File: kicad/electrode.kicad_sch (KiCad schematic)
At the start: 0 parts

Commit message: mcu changed cuz of clock requierements
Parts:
- added C1: 0.1u, symbol Device:C
- added C2: 4.7u, symbol Device:C
- added U1: CH32L103K8U6, easyeda2kicad:QFN-32_L4.0-W4.0-P0.40-BL-EP2.7-A, symbol LIB:CH32L103K8U6
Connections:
- new net 3v3: C1.1, C2.1, U1.1 (VDD)
- new net GND: C1.2, C2.2, U1.33 (EP)

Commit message: new mcu with clk_out and layout draft
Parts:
- C1: footprint (none) -> Capacitor_SMD:C_0402_1005Metric
- C2: footprint (none) -> Capacitor_SMD:C_0603_1608Metric
- U1: footprint easyeda2kicad:QFN-32_L4.0-W4.0-P0.40-BL-EP2.7-A -> LIB:QFN-32_L4.0-W4.0-P0.40-BL-EP2.7-A
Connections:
- net CLK_OUT: now reaches U1.18 (PA8)
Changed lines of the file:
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@@
+	(wire
+		(pts
+			(xy 186.69 110.49) (xy 168.91 110.49)
+		)
+		(stroke
+			(width 0)
+			(type default)
+		)
+	)
 	(wire
 		(pts
@@
 			)
 			(justify right)
+		)
+	)
+	(hierarchical_label "CLK_OUT"
+		(shape input)
+		(at 186.69 110.49 0)
+		(effects
+			(font
+				(size 1.27 1.27)
+			)
+			(justify left)
 		)
 	)
@@
 			)
 		)
-		(property "Footprint" "easyeda2kicad:QFN-32_L4.0-W4.0-P0.40-BL-EP2.7-A"
+		(property "Footprint" "LIB:QFN-32_L4.0-W4.0-P0.40-BL-EP2.7-A"
 			(at 142.24 138.43 0)
 			(hide yes)
@@
 			)
 		)
-		(property "Footprint" ""
+		(property "Footprint" "Capacitor_SMD:C_0402_1005Metric"
 			(at 134.3152 44.45 0)
 			(hide yes)
@@
 			)
 		)
-		(property "Footprint" ""
+		(property "Footprint" "Capacitor_SMD:C_0603_1608Metric"
 			(at 149.5552 44.45 0)
 			(hide yes)

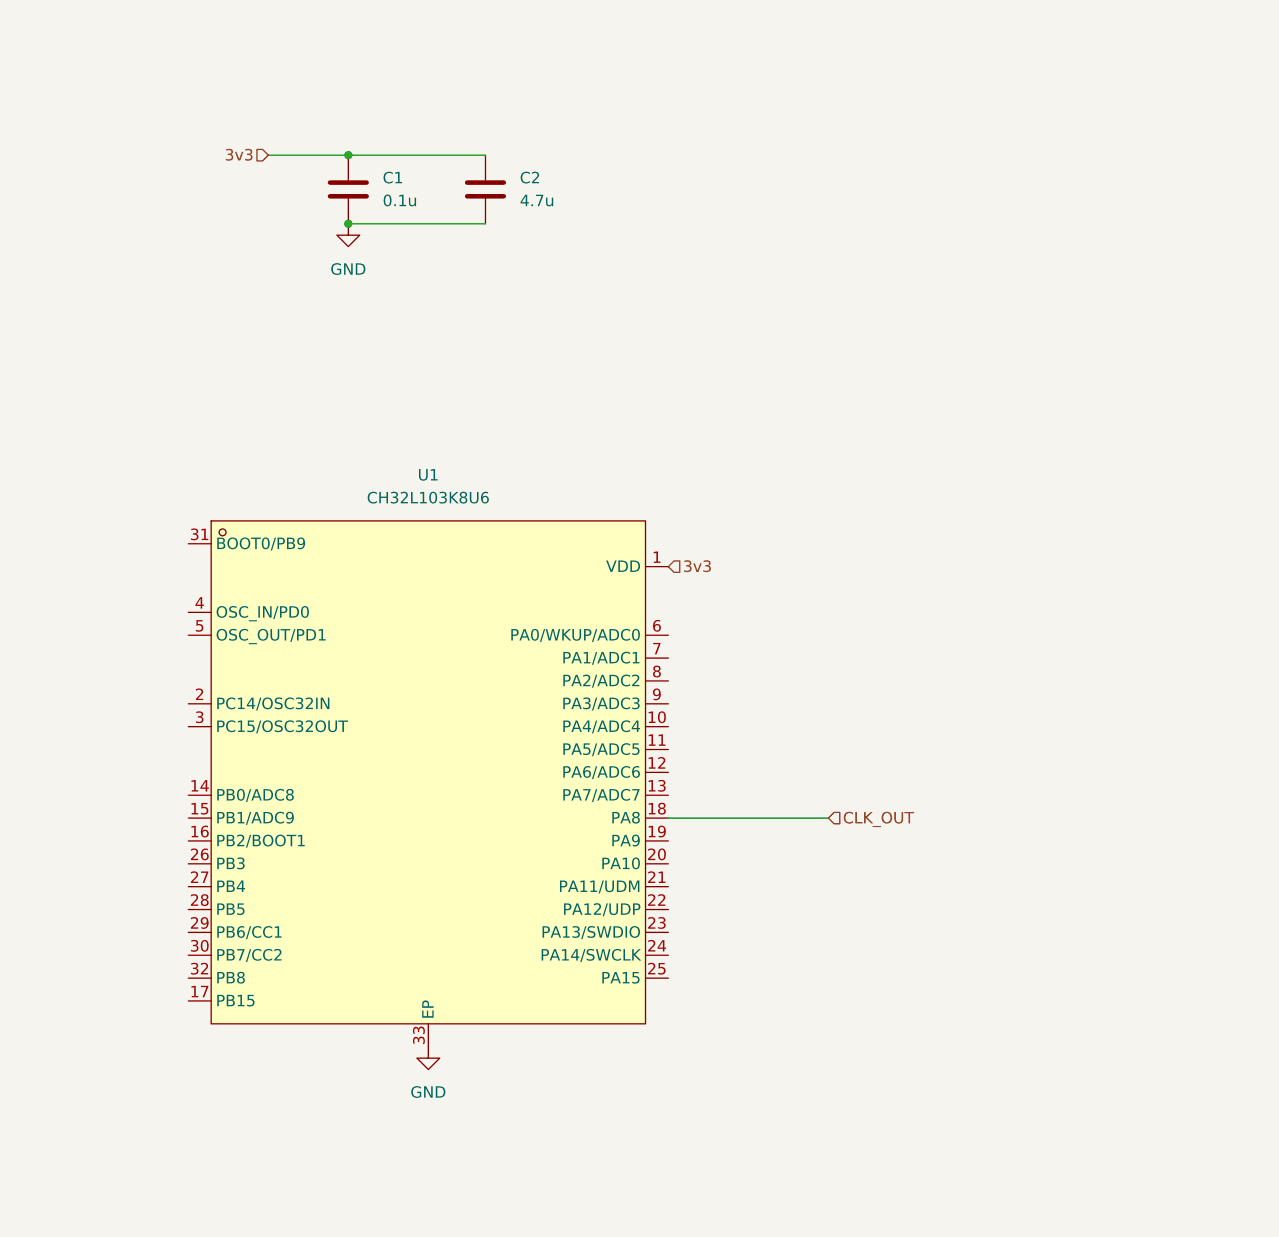
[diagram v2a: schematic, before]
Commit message: mcu chain test board with mcu side only for now
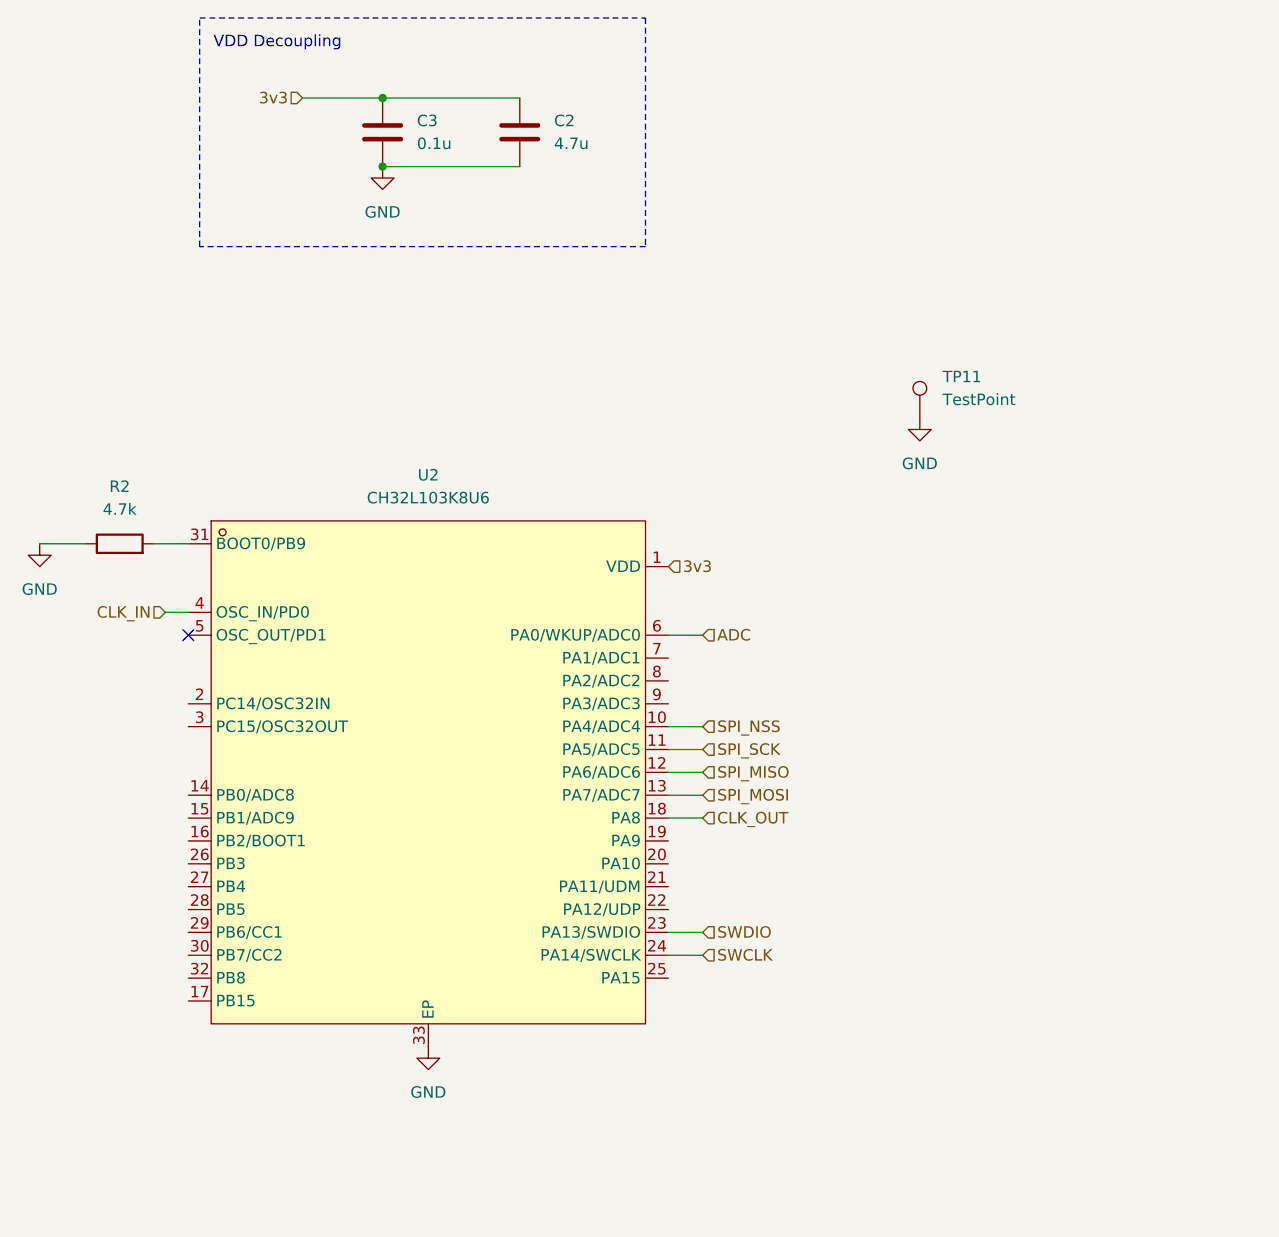
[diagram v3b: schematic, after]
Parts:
- added R2: 4.7k, symbol Device:R
- added TP11: TestPoint, symbol Connector:TestPoint
- renumbered C1 to C3, U1 to U2
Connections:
- net GND: now also R2.1, TP11.1
- net SPI_NSS: now reaches U2.10 (PA4/ADC4)
- net SPI_SCK: now reaches U2.11 (PA5/ADC5)
- net SPI_MISO: now reaches U2.12 (PA6/ADC6)
- net SPI_MOSI: now reaches U2.13 (PA7/ADC7)
- net SWDIO: now reaches U2.23 (PA13/SWDIO)
- net SWCLK: now reaches U2.24 (PA14/SWCLK)
- net at U2.31 (BOOT0/PB9): now also R2.2
- net CLK_IN: now reaches U2.4 (OSC_IN/PD0)
- net ADC: now reaches U2.6 (PA0/WKUP/ADC0)
- no-connect marks 0 -> 1
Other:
- note added: "VDD Decoupling"
- moved on the sheet: C2, C3

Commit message: I dont remember last commit idk
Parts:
- added D1: LED, LED_SMD:LED_0603_1608Metric, symbol Device:LED
- added R11: 470, Resistor_SMD:R_0603_1608Metric, symbol Device:R
- added R14: R, symbol Device:R
- added R8: 10k, Resistor_SMD:R_0603_1608Metric, symbol Device:R
- added TP16, TP19, TP22: TestPoint, TestPoint:TestPoint_Pad_2.5x2.5mm, symbol Connector:TestPoint
- C2: LCSC Part (none) -> C19666
- C3: LCSC Part (none) -> C1525
- R2: footprint (none) -> Resistor_SMD:R_0603_1608Metric; LCSC Part (none) -> C23162
- TP11: footprint (none) -> TestPoint:TestPoint_Pad_2.5x2.5mm; now left out of the parts list
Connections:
- net GND: now also D1.1 (K), R8.1
- net SPI_MISO: now also U2.27 (PB4); no longer U2.12 (PA6/ADC6)
- net SPI_MOSI: now also U2.28 (PB5), R8.2; no longer U2.13 (PA7/ADC7)
- net SPI_NSS: now also U2.25 (PA15); no longer U2.10 (PA4/ADC4)
- net SPI_SCK: now also U2.26 (PB3); no longer U2.11 (PA5/ADC5)
- net at U2.15 (PB1/ADC9): now also TP16.1
- net at U2.19 (PA9): now also TP19.1
- net at U2.20 (PA10): now also TP22.1
- net at U2.32 (PB8): now also R11.1
- net ADC: no longer names the net of U2.6 (PA0/WKUP/ADC0)
- new net: D1.2 (A), R11.2
- new net OPA_N: U2.11 (PA5/ADC5)
- new net OPA_OUT: U2.10 (PA4/ADC4)
- new net OPA_P: U2.12 (PA6/ADC6)
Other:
- note added: "UART_RX"
- note added: "UART_TX"
